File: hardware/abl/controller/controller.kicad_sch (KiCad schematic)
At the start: 27 parts, among them IC1 LSF0204PWJ, IC2 FXL6408UMX, IC3 VEML6040A3OG, IC4 FXL6408UMX, J1 SFW20S-2STE1LF, J2 Conn_02x03_Odd_Even, J3 Conn_02x03_Odd_Even, J4 PRT-14417, J5 Conn_02x04_Odd_Even, Q2 AO3401A, Q4 AO3401A, U1 INA219AxD

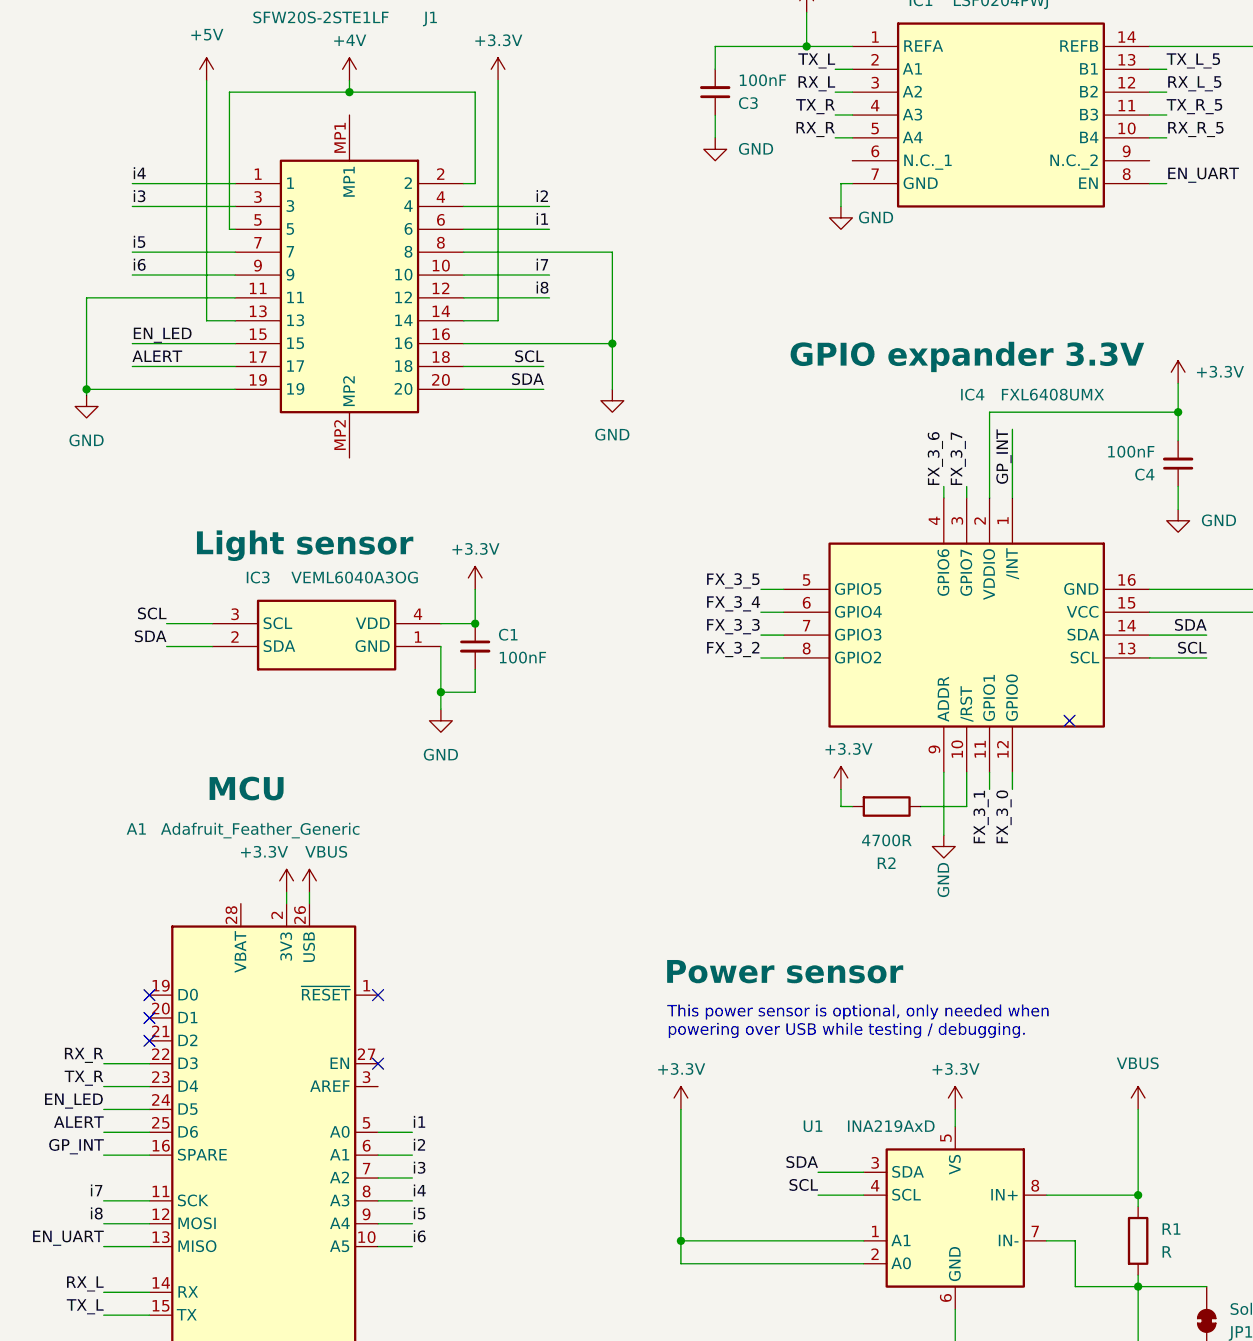
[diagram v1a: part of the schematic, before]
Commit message: Adjusted pin assignment of i1 to i4, rotated the flex connector, and rerouted most of the long traces.
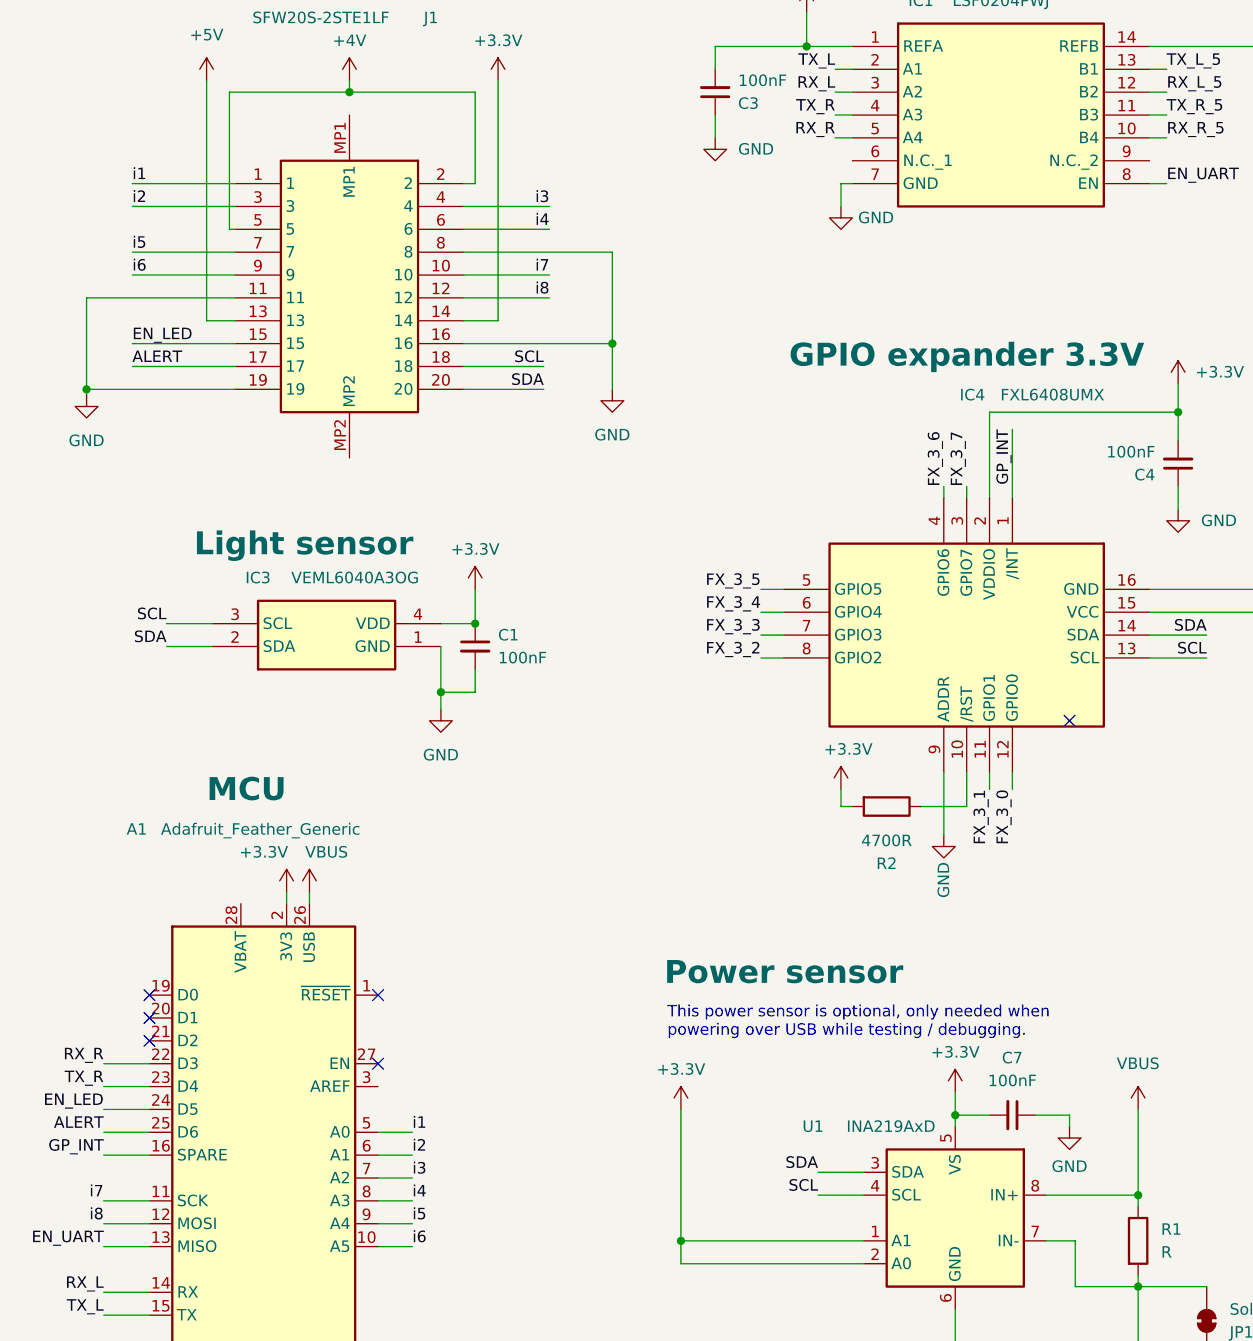
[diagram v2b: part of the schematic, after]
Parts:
- added C7: 100nF, Capacitor_SMD:C_0402_1005Metric, symbol Device:C_Small
- J4: LCSC Part # (none) -> C160404
- Q2, Q4: LCSC Part # (none) -> C15127; Purpose (none) -> Switch sensor power
- R2, R3: footprint Resistor_SMD:R_0603_1608Metric_Pad0.98x0.95mm_HandSolder -> Resistor_SMD:R_0402_1005Metric; LCSC Part # C23162 -> C25900
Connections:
- net +3.3V: now also C7.2
- net GND: now also C7.1
- net i1: now also J1.1; no longer J1.6
- net i2: now also J1.3; no longer J1.4
- net i3: now also J1.4; no longer J1.3
- net i4: now also J1.6; no longer J1.1

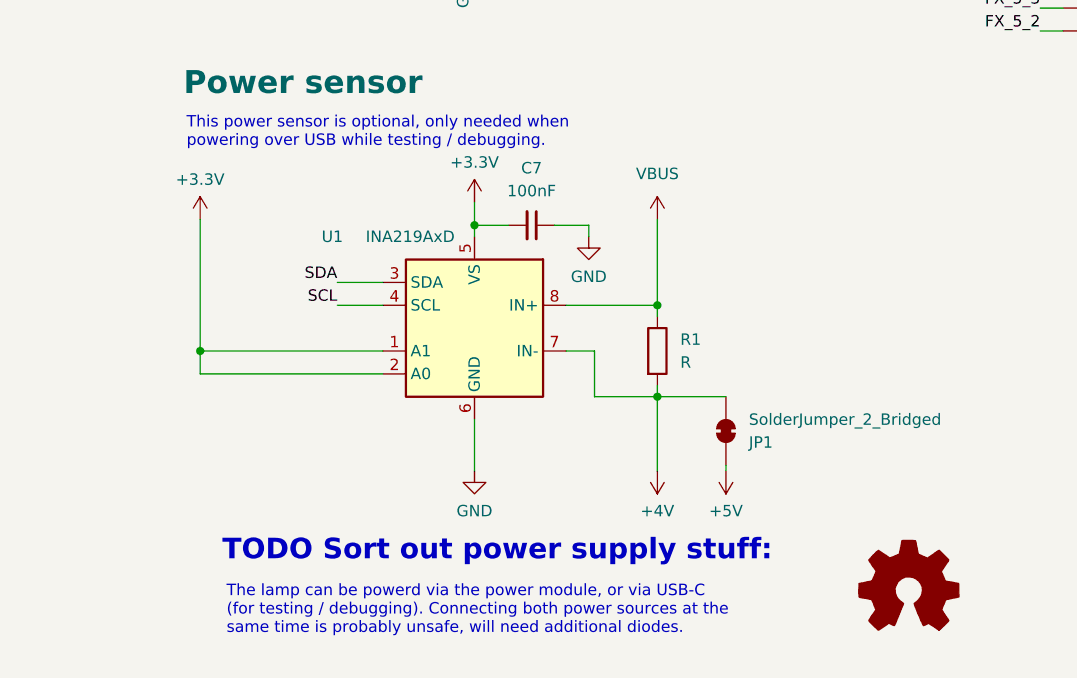
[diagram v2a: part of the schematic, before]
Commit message: Finally added the missing schottky diode and re-layoutet the power area.
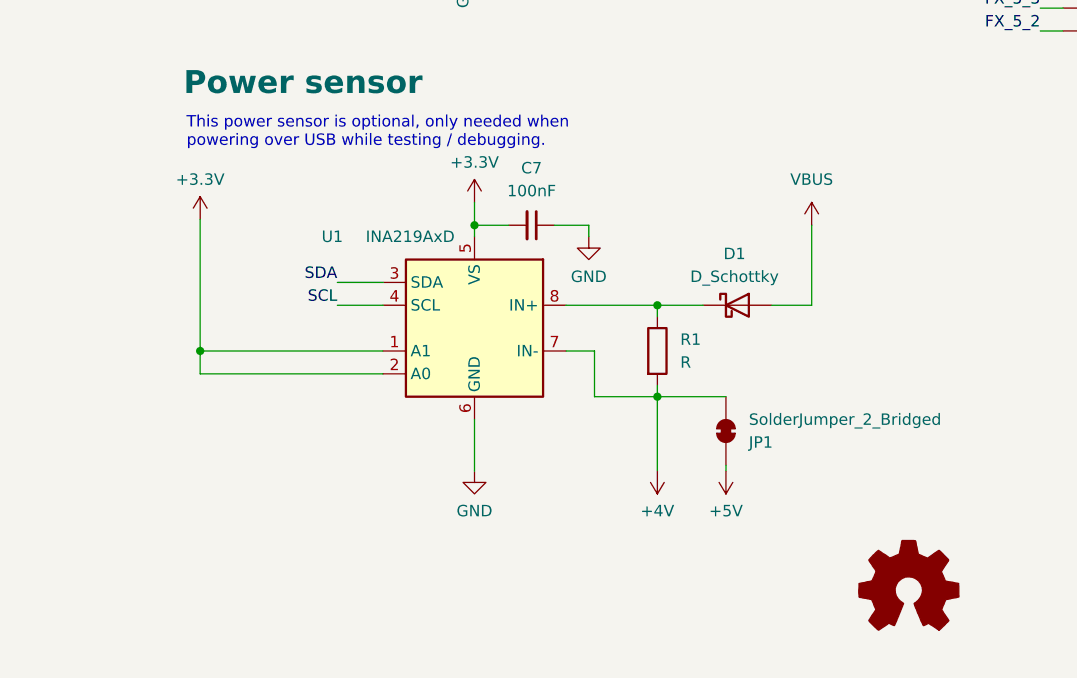
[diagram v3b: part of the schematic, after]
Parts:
- added D1: D_Schottky, Own footprints:YFW SSL34F Schottky Diode, symbol Device:D_Schottky
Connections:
- net VBUS: now also D1.2 (A); no longer R1.1, U1.8 (IN+)
- new net: D1.1 (K), R1.1, U1.8 (IN+)
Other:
- note removed: "TODO Sort out power supply stuff:"
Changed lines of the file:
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@@
 	)
 	(junction
+		(at 138.43 157.48)
+		(diameter 0)
+		(color 0 0 0 0)
+	)
+	(junction
 		(at 64.77 93.98)
 		(diameter 0)
@@
 	)
 	(junction
-		(at 138.43 157.48)
-		(diameter 0)
-		(color 0 0 0 0)
-	)
-	(junction
 		(at 60.96 101.6)
 		(diameter 0)
@@
 	(wire
 		(pts
+			(xy 138.43 157.48) (xy 143.51 157.48)
+		)
+		(stroke
+			(width 0)
+			(type default)
+		)
+	)
+	(wire
+		(pts
 			(xy 64.77 90.17) (xy 64.77 93.98)
 		)
@@
 	(wire
 		(pts
+			(xy 155.575 148.59) (xy 155.575 157.48)
+		)
+		(stroke
+			(width 0)
+			(type default)
+		)
+	)
+	(wire
+		(pts
+			(xy 155.575 157.48) (xy 151.13 157.48)
+		)
+		(stroke
+			(width 0)
+			(type default)
+		)
+	)
+	(wire
+		(pts
 			(xy 269.875 42.545) (xy 267.97 42.545)
 		)
@@
 	(wire
 		(pts
-			(xy 138.43 147.955) (xy 138.43 157.48)
-		)
-		(stroke
-			(width 0)
-			(type default)
-		)
-	)
-	(wire
-		(pts
 			(xy 229.87 65.405) (xy 229.87 66.675)
 		)
@@
 		)
 	)
-	(text_box "The lamp can be powerd via the power module, or via USB-C (for testing / debugging). Connecting both power sources at the same time is probably unsafe, will need additional diodes."
-		(exclude_from_sim no)
-		(at 89.535 187.325 0)
-		(size 66.04 10.16)
-		(stroke
-			(width -0.0001)
-			(type default)
-		)
-		(fill
-			(type none)
-		)
-		(effects
-			(font
-				(size 1.27 1.27)
-			)
-			(justify left top)
-		)
-	)
 	(text_box "This power sensor is optional, only needed when powering over USB while testing / debugging."
 		(exclude_from_sim no)
@@
 		)
 	)
-	(text "TODO Sort out power supply stuff:"
-		(exclude_from_sim no)
-		(at 120.65 184.785 0)
-		(effects
-			(font
-				(size 2.286 2.286)
-				(thickness 0.4572)
-				(bold yes)
-				(color 255 0 4 1)
-			)
-		)
-	)
 	(label "RX_L"
 		(at 193.675 50.8 90)
@@
 	(symbol
 		(lib_id "power:VBUS")
-		(at 138.43 147.955 0)
+		(at 155.575 148.59 0)
 		(unit 1)
 		(exclude_from_sim no)
@@
 		(fields_autoplaced yes)
 		(property "Reference" "#PWR036"
-			(at 138.43 151.765 0)
+			(at 155.575 152.4 0)
 			(effects
 				(font
@@
 		)
 		(property "Value" "VBUS"
-			(at 138.43 142.875 0)
+			(at 155.575 143.51 0)
 			(effects
 				(font
@@
 		)
 		(property "Footprint" ""
-			(at 138.43 147.955 0)
+			(at 155.575 148.59 0)
 			(effects
 				(font
@@
 		)
 		(property "Datasheet" ""
-			(at 138.43 147.955 0)
+			(at 155.575 148.59 0)
 			(effects
 				(font
@@
 		)
 		(property "Description" "Power symbol creates a global label with name \"VBUS\""
-			(at 138.43 147.955 0)
+			(at 155.575 148.59 0)
 			(effects
 				(font
@@
 					(unit 1)
 				)
+			)
+		)
+	)
+	(symbol
+		(lib_id "Device:D_Schottky")
+		(at 147.32 157.48 0)
+		(unit 1)
+		(exclude_from_sim no)
+		(in_bom yes)
+		(on_board yes)
+		(dnp no)
+		(fields_autoplaced yes)
+		(property "Reference" "D1"
+			(at 147.0025 151.765 0)
+			(effects
+				(font
+					(size 1.27 1.27)
+				)
+			)
+		)
+		(property "Value" "D_Schottky"
+			(at 147.0025 154.305 0)
+			(effects
+				(font
+					(size 1.27 1.27)
+				)
+			)
+		)
+		(property "Footprint" "Own footprints:YFW SSL34F Schottky Diode"
+			(at 147.32 157.48 0)
+			(effects
+				(font
+					(size 1.27 1.27)
+				)
+				(hide yes)
+			)
+		)
+		(property "Datasheet" "~"
+			(at 147.32 157.48 0)
+			(effects
+				(font
+					(size 1.27 1.27)
+				)
+				(hide yes)
+			)
+		)
+		(property "Description" "Schottky diode"
+			(at 147.32 157.48 0)
+			(effects
+				(font
+					(size 1.27 1.27)
+				)
+				(hide yes)
+			)
+		)
+		(property "LCSC Part #" "C1884559"
+			(at 147.32 157.48 0)
+			(effects
+				(font
+					(size 1.27 1.27)
+				)
+				(hide yes)
+			)
+		)
+		(pin "2"
+		)
+		(pin "1"
+		)
+		(instances
+			(project "Controller"
+				(path "/19e0c2ec-2e53-449d-b0ad-9539b125a162"
+					(reference "D1")
+					(unit 1)
+				)

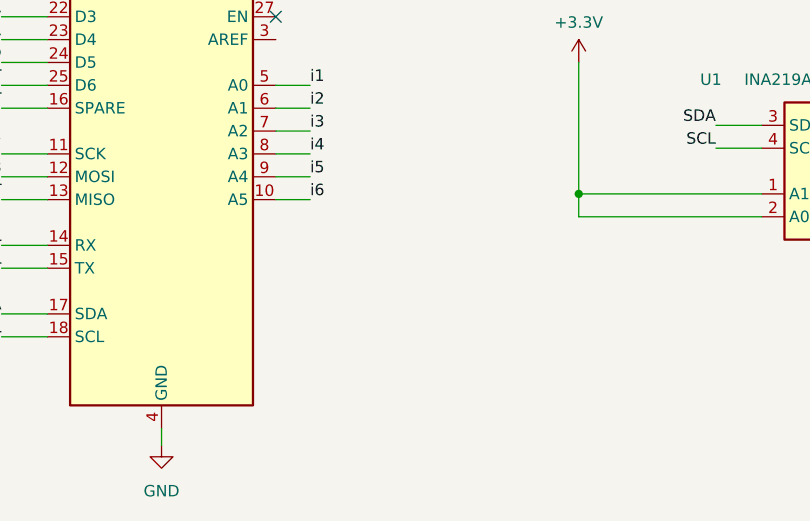
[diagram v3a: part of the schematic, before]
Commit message: Added pull ups for I2C.
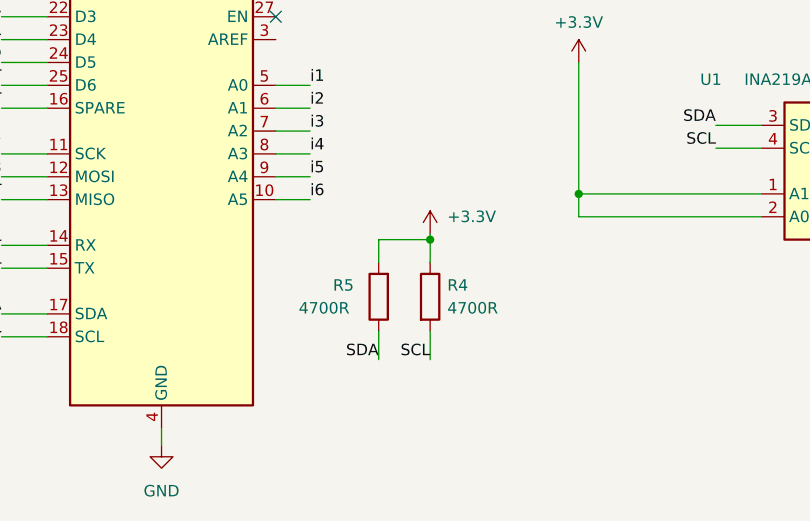
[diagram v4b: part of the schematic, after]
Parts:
- added R4, R5: 4700R, Resistor_SMD:R_0402_1005Metric, symbol Device:R
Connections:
- net +3.3V: now also R4.1, R5.2
- net SCL: now also R4.2
- net SDA: now also R5.1
